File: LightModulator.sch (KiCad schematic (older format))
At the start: 65 parts, among them Q1 BT136-600, Q2 BT136-600, Q3 BT136-600, Q4 BT136-600, Q5 BT136-600, Q6 BT136-600, U1 CD4017BE, U2 CD4093BE

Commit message: Correction et simulation
Correction du schéma: le snubber n'était pas bien positionné
Simulation de l'alimentation sous LtSpice pour vérifier ce qui est envoyé aux TRIAC.
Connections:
- net LINE: no longer C1.1, C2.1, C3.1, C4.1, C5.1, C6.1
- net at B1.1 (Pin_1), Q1.2 (A2): now also C1.1
- net at B2.1 (Pin_1), Q2.2 (A2): now also C2.1
- net at B3.1 (Pin_1), Q3.2 (A2): now also C3.1
- net at B4.1 (Pin_1), Q4.2 (A2): now also C4.1
- net at B5.1 (Pin_1), Q5.2 (A2): now also C5.1
- net at B6.1 (Pin_1), Q6.2 (A2): now also C6.1
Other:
- note added: "68k @50Hz"
- moved on the sheet: B1, B2, B3, B4, B5, B6

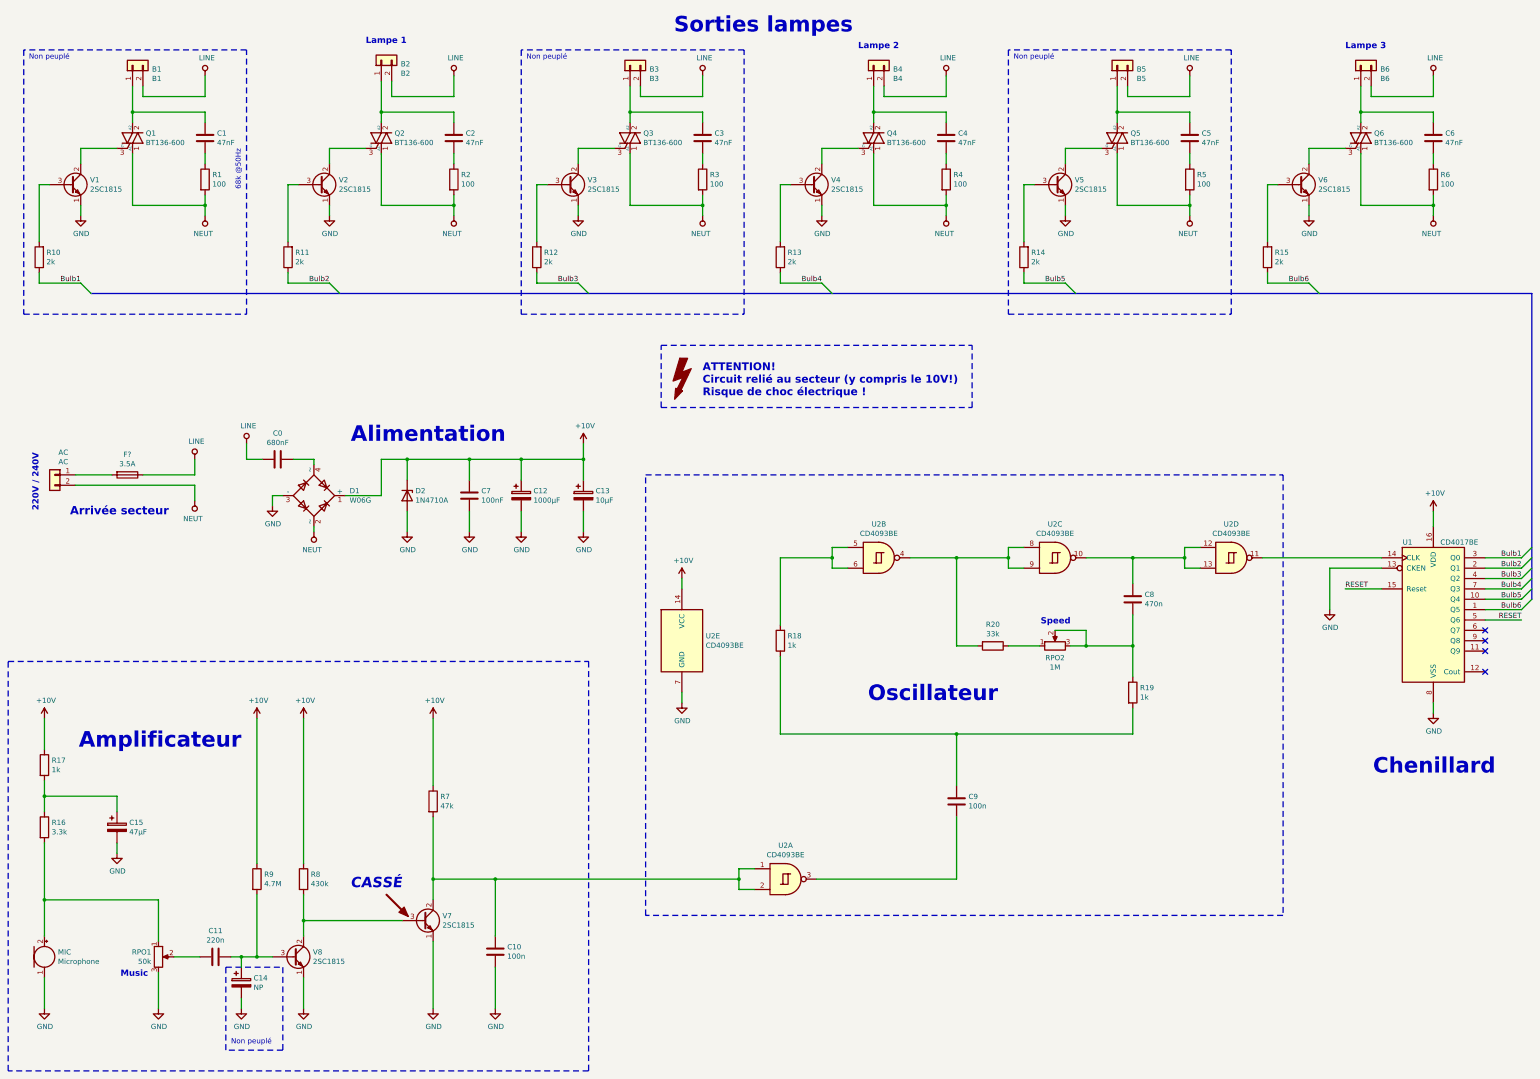
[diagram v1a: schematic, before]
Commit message: Ajout illustrations et ERC ok
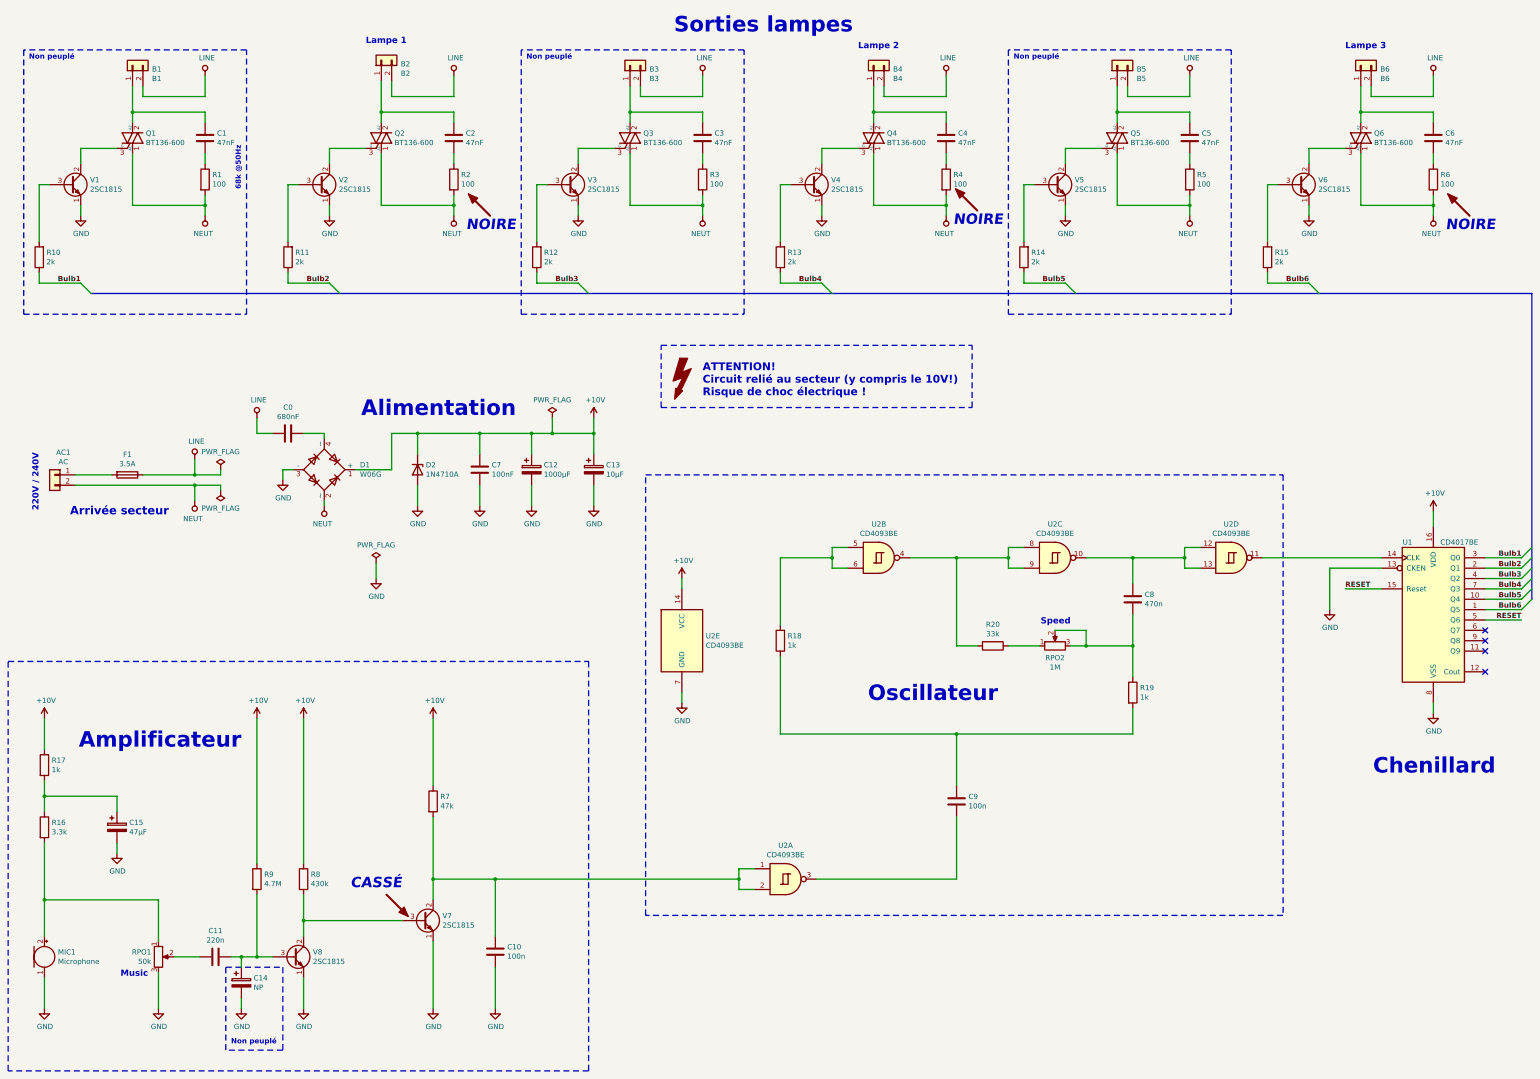
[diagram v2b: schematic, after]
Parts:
- gave numbers to parts that had none: 1
- renumbered AC to AC1, MIC to MIC1
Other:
- note added: "NOIRE"
- moved on the sheet: C0, C12, C13, C7, D1, D2
